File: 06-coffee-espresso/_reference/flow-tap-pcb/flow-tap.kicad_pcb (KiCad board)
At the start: 2 copper layers, 35.6 x 23.6 mm, 5 parts, among them J1 GICAR_meter, J2 to_Vivaldi, J3 to_ito, U1 74LVC1G17

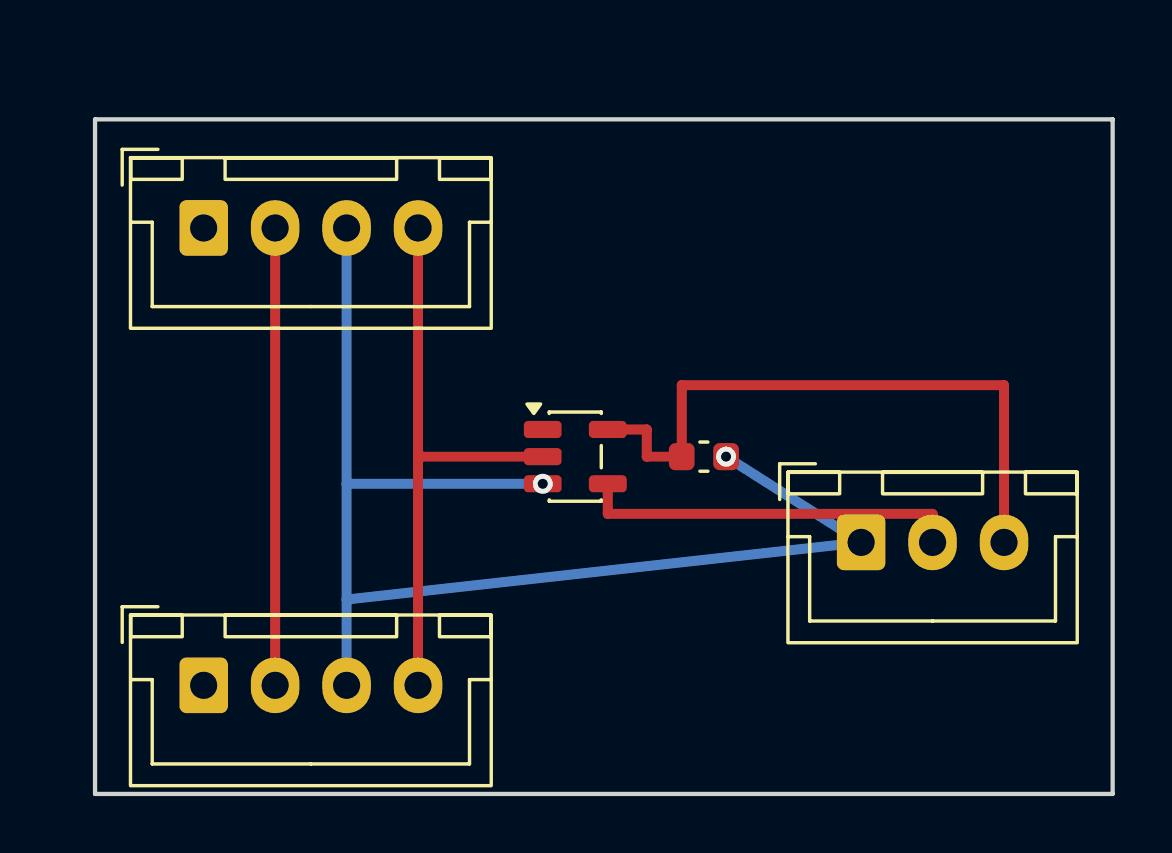
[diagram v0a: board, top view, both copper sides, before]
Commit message: refactor(06-015): compact the flow-tap layout ~46% smaller
Rotate the three connectors vertical and pack them in a row along the bottom with
the buffer + cap up top. Board drops from 35.6x23.6 (840 mm^2) to 23.1x19.8
(457 mm^2). Still DRC-clean: 0 violations, 0 unconnected. Same nets/topology
(signals F.Cu, GND B.Cu); re-exported Gerbers + render.

Fixed a rotation-transform sign bug in the generator (KiCad's footprint-rotation
convention is rx=ox+px*cos+py*sin, ry=oy-px*sin+py*cos) so rotated footprints
place correctly.

Co-Authored-By: Claude Opus 4.8 <noreply@anthropic.com>
Claude-Session: https://claude.ai/code/session_01NfkRErMrPyNuft1RbpzMet
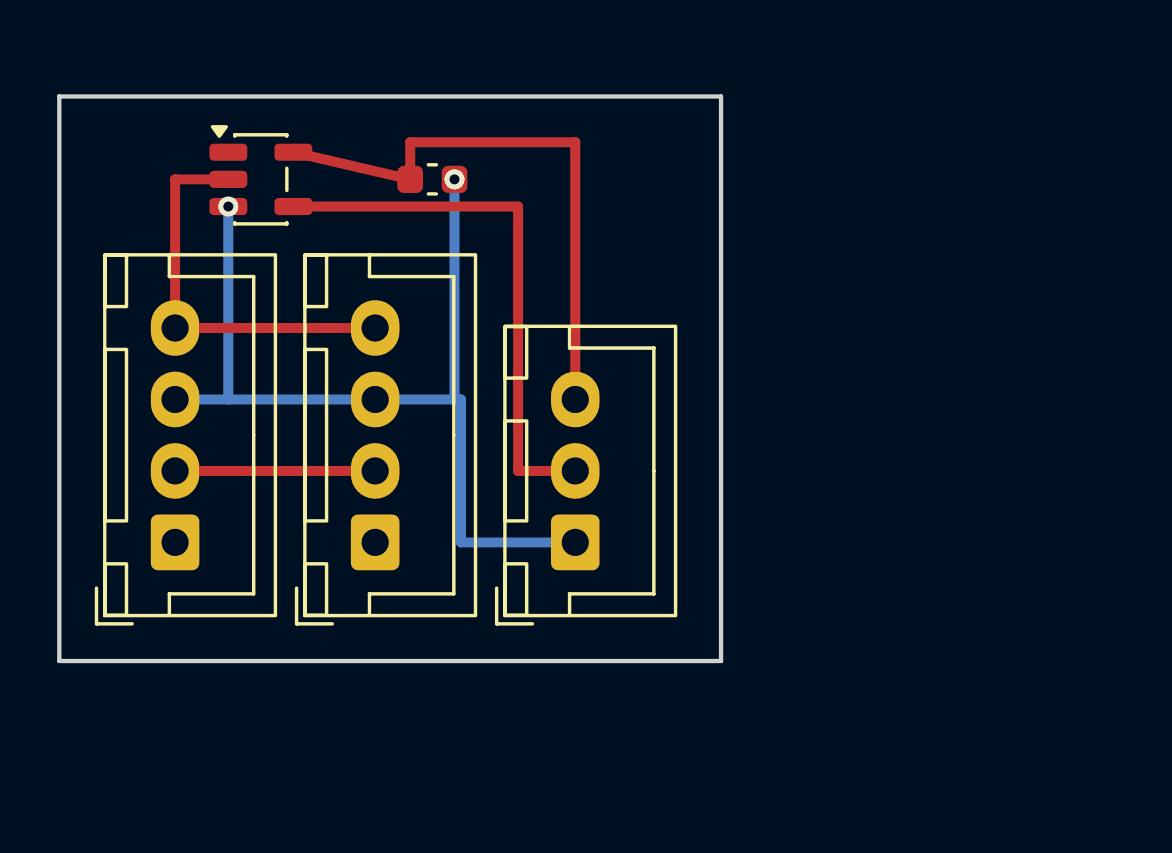
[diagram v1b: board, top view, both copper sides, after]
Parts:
- moved U1 14.7 mm to (7.00, 1.30)
- moved C1 13.6 mm to (13.0, 1.30)
- moved J1 11.0 mm to (4.00, 14.0), turned to 90 degrees
- moved J3 10.0 mm to (18.0, 14.0), turned to 90 degrees
- moved J2 7.81 mm to (11.0, 14.0), turned to 90 degrees
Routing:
- net GND: track 46.6 -> 33.5 mm
- net N_PLUS: track 16.0 -> 7.00 mm
- net N_O: track 20.4 -> 14.1 mm
- net N_OUT: track 13.4 -> 19.1 mm
- net V5: track 22.8 -> 20.3 mm
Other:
- board size 35.6 x 23.6 mm -> 23.2 x 19.8 mm

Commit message: refactor(06-015): 45-degree trace corners on the flow-tap board
Chamfer every 90-degree corner into two 45-degree bends. Still DRC-clean
(0 violations, 0 unconnected). Re-exported Gerbers + render.

Co-Authored-By: Claude Opus 4.8 <noreply@anthropic.com>
Claude-Session: https://claude.ai/code/session_01NfkRErMrPyNuft1RbpzMet
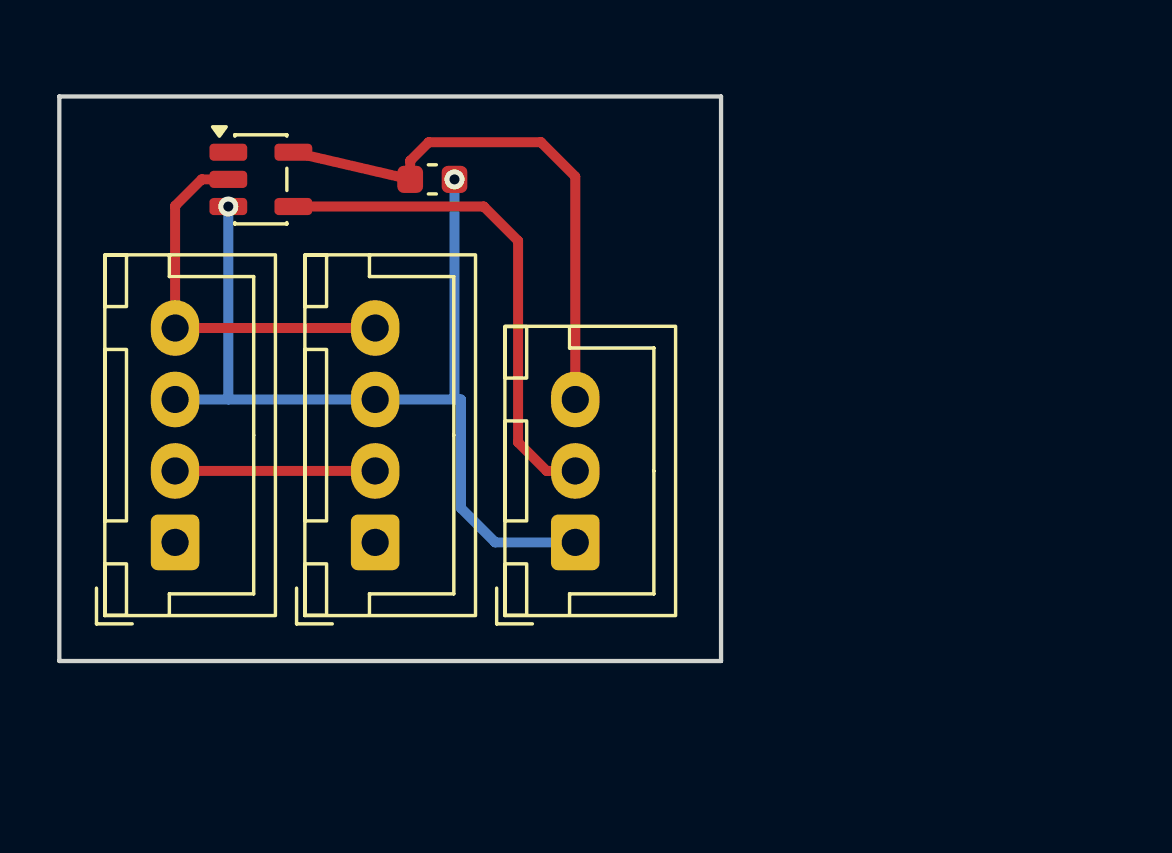
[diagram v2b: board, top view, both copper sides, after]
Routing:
- net N_OUT: track 19.1 -> 17.8 mm
- net V5: track 20.3 -> 19.2 mm
- net GND: track 33.5 -> 32.7 mm
- net N_O: track 14.1 -> 13.5 mm
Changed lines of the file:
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@@
   (segment (start 4.0 11.5) (end 11.0 11.5) (width 0.35) (layer "F.Cu") (net 2))
   (segment (start 4.0 6.5) (end 11.0 6.5) (width 0.35) (layer "F.Cu") (net 3))
-  (segment (start 4.0 6.5) (end 4.0 1.3) (width 0.35) (layer "F.Cu") (net 3))
-  (segment (start 4.0 1.3) (end 5.8625 1.3) (width 0.35) (layer "F.Cu") (net 3))
+  (segment (start 4.0 6.5) (end 4.0 2.2313) (width 0.35) (layer "F.Cu") (net 3))
+  (segment (start 4.0 2.2313) (end 4.9313 1.3) (width 0.35) (layer "F.Cu") (net 3))
+  (segment (start 4.9313 1.3) (end 5.8625 1.3) (width 0.35) (layer "F.Cu") (net 3))
   (segment (start 8.1375 0.35) (end 12.225 1.3) (width 0.35) (layer "F.Cu") (net 4))
-  (segment (start 12.225 1.3) (end 12.225 0.0) (width 0.35) (layer "F.Cu") (net 4))
-  (segment (start 12.225 0.0) (end 18.0 0.0) (width 0.35) (layer "F.Cu") (net 4))
-  (segment (start 18.0 0.0) (end 18.0 9.0) (width 0.35) (layer "F.Cu") (net 4))
-  (segment (start 8.1375 2.25) (end 16.0 2.25) (width 0.35) (layer "F.Cu") (net 5))
-  (segment (start 16.0 2.25) (end 16.0 11.5) (width 0.35) (layer "F.Cu") (net 5))
-  (segment (start 16.0 11.5) (end 18.0 11.5) (width 0.35) (layer "F.Cu") (net 5))
+  (segment (start 12.225 1.3) (end 12.225 0.65) (width 0.35) (layer "F.Cu") (net 4))
+  (segment (start 12.225 0.65) (end 12.875 0.0) (width 0.35) (layer "F.Cu") (net 4))
+  (segment (start 12.875 0.0) (end 16.8 0.0) (width 0.35) (layer "F.Cu") (net 4))
+  (segment (start 16.8 0.0) (end 18.0 1.2) (width 0.35) (layer "F.Cu") (net 4))
+  (segment (start 18.0 1.2) (end 18.0 9.0) (width 0.35) (layer "F.Cu") (net 4))
+  (segment (start 8.1375 2.25) (end 14.8 2.25) (width 0.35) (layer "F.Cu") (net 5))
+  (segment (start 14.8 2.25) (end 16.0 3.45) (width 0.35) (layer "F.Cu") (net 5))
+  (segment (start 16.0 3.45) (end 16.0 10.5) (width 0.35) (layer "F.Cu") (net 5))
+  (segment (start 16.0 10.5) (end 17.0 11.5) (width 0.35) (layer "F.Cu") (net 5))
+  (segment (start 17.0 11.5) (end 18.0 11.5) (width 0.35) (layer "F.Cu") (net 5))
   (segment (start 4.0 9.0) (end 14.0 9.0) (width 0.35) (layer "B.Cu") (net 1))
-  (segment (start 14.0 9.0) (end 14.0 14.0) (width 0.35) (layer "B.Cu") (net 1))
-  (segment (start 14.0 14.0) (end 18.0 14.0) (width 0.35) (layer "B.Cu") (net 1))
+  (segment (start 14.0 9.0) (end 14.0 12.8) (width 0.35) (layer "B.Cu") (net 1))
+  (segment (start 14.0 12.8) (end 15.2 14.0) (width 0.35) (layer "B.Cu") (net 1))
+  (segment (start 15.2 14.0) (end 18.0 14.0) (width 0.35) (layer "B.Cu") (net 1))
   (via (at 5.8625 2.25) (size 0.7) (drill 0.35) (layers "F.Cu" "B.Cu") (net 1))
   (segment (start 5.8625 2.25) (end 5.8625 9.0) (width 0.35) (layer "B.Cu") (net 1))

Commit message: feat(pcb): add silkscreen reference designators to both boards
Both generated boards previously exported empty silkscreen layers. Add
refdes for every part plus LED polarity marks so the boards can be hand-
assembled and inspected without cross-referencing the schematic.

flow-tap: J1/U1/J2/C1/J3 in a clean row above the pad field.

ir-blaster (xiao-c3-ir-rf): D1-D3 (with a cathode bar on the pin-1/west
side of each LED), R1-R5, C1-C4, Q1, A1 (XIAO), and M1 mirrored on
B.SilkS above the E07 header (the module mounts on the back).

Regenerated boards, gerbers, and top/bottom renders. DRC 0 violations /
0 unconnected on both.

Co-Authored-By: Claude Opus 4.8 <noreply@anthropic.com>
Claude-Session: https://claude.ai/code/session_01NfkRErMrPyNuft1RbpzMet
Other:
- board text added: "C1"
- board text added: "J1"
- board text added: "J2"
- board text added: "J3"
- board text added: "U1"
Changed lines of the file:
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@@
     )
+  )
+  (gr_text "J1" (at 4 -0.9) (layer "F.SilkS")
+    (effects (font (size 0.8 0.8) (thickness 0.12)))
+  )
+  (gr_text "U1" (at 7 -0.9) (layer "F.SilkS")
+    (effects (font (size 0.8 0.8) (thickness 0.12)))
+  )
+  (gr_text "J2" (at 11 -0.9) (layer "F.SilkS")
+    (effects (font (size 0.8 0.8) (thickness 0.12)))
+  )
+  (gr_text "C1" (at 13 -0.9) (layer "F.SilkS")
+    (effects (font (size 0.8 0.8) (thickness 0.12)))
+  )
+  (gr_text "J3" (at 18 -0.9) (layer "F.SilkS")
+    (effects (font (size 0.8 0.8) (thickness 0.12)))
   )
   (gr_line (start -0.05 -1.6) (end 23.1 -1.6) (layer "Edge.Cuts") (width 0.15))

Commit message: fix(pcb): address silkscreen critique — drop redundant LED bars, thicker silk
- ir-blaster: remove the free-floating cathode bars; LED_D5.0mm already
  renders a cathode flat on the pin-1/west side, so the bars were a
  redundant, cosmetically nonstandard second mark. Correct the misleading
  "custom fps carry no silk" comment (they're stock fps with a hidden
  Reference; their geometric silk does render).
- both: bump silk stroke to >=0.15 mm (was 0.12 mm) to clear the common
  JLCPCB minimum so thin text can't print broken.
- flow-tap: fold the silk-text extents into the auto-outline so the top
  refdes row can't be clipped if pad/courtyard bounds shrink (outline is
  now 23.1 x 21.0 mm).

Regenerated boards, gerbers, renders. DRC 0/0 on both.

Co-Authored-By: Claude Opus 4.8 <noreply@anthropic.com>
Claude-Session: https://claude.ai/code/session_01NfkRErMrPyNuft1RbpzMet
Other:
- board size 23.2 x 19.8 mm -> 23.2 x 21 mm
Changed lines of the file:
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@@
   )
   (gr_text "J1" (at 4 -0.9) (layer "F.SilkS")
-    (effects (font (size 0.8 0.8) (thickness 0.12)))
+    (effects (font (size 0.8 0.8) (thickness 0.15)))
   )
   (gr_text "U1" (at 7 -0.9) (layer "F.SilkS")
-    (effects (font (size 0.8 0.8) (thickness 0.12)))
+    (effects (font (size 0.8 0.8) (thickness 0.15)))
   )
   (gr_text "J2" (at 11 -0.9) (layer "F.SilkS")
-    (effects (font (size 0.8 0.8) (thickness 0.12)))
+    (effects (font (size 0.8 0.8) (thickness 0.15)))
   )
   (gr_text "C1" (at 13 -0.9) (layer "F.SilkS")
-    (effects (font (size 0.8 0.8) (thickness 0.12)))
+    (effects (font (size 0.8 0.8) (thickness 0.15)))
   )
   (gr_text "J3" (at 18 -0.9) (layer "F.SilkS")
-    (effects (font (size 0.8 0.8) (thickness 0.12)))
+    (effects (font (size 0.8 0.8) (thickness 0.15)))
   )
-  (gr_line (start -0.05 -1.6) (end 23.1 -1.6) (layer "Edge.Cuts") (width 0.15))
-  (gr_line (start 23.1 -1.6) (end 23.1 18.15) (layer "Edge.Cuts") (width 0.15))
+  (gr_line (start -0.05 -2.9) (end 23.1 -2.9) (layer "Edge.Cuts") (width 0.15))
+  (gr_line (start 23.1 -2.9) (end 23.1 18.15) (layer "Edge.Cuts") (width 0.15))
   (gr_line (start 23.1 18.15) (end -0.05 18.15) (layer "Edge.Cuts") (width 0.15))
-  (gr_line (start -0.05 18.15) (end -0.05 -1.6) (layer "Edge.Cuts") (width 0.15))
+  (gr_line (start -0.05 18.15) (end -0.05 -2.9) (layer "Edge.Cuts") (width 0.15))
   (segment (start 4.0 11.5) (end 11.0 11.5) (width 0.35) (layer "F.Cu") (net 2))
   (segment (start 4.0 6.5) (end 11.0 6.5) (width 0.35) (layer "F.Cu") (net 3))
